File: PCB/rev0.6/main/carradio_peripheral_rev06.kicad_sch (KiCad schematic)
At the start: 205 parts, among them J1 ISO 10487 A (via pigtail), J10 K-line module socket, J12 Display buttons, J13 HDMI in (from VIM3), J14 Display FPC 40P 0.5mm, J18 VIM3 VIN (JST-XH 2P), J2 VIM3 40-pin via 2x20 IDC ribb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, J21 Expansion 2, J22 SWD, J23 Audio module socket, J25 USB module socket, J27 GNSS module socket, J5 VIM3 POWER key lead, J7 BH1750 light sensor, J8 ISO 10487 C1 (via pigtail), Q1 AO3400A, Q10 P-MOSFET -40V, Q11 CSD18543Q3A, Q12 CSD18543Q3A, Q2 P-MOSFET -60V, Q3 2N7002, SW1 BOOTSEL, SW2 RESET, U1 TPS560430XDBVR, U12 TPS55288RPMR, U13 CH334R, U19 AP2112K-3.3, U2 EL817S1(C), U20 RP2350B, U21 W25Q128JVS, U3 EL817S1(C), U4 EL817S1(C), U5 EL817S1(C), U6 LP5907MFX-3.3, Y1 12MHz, Y3 12MHz

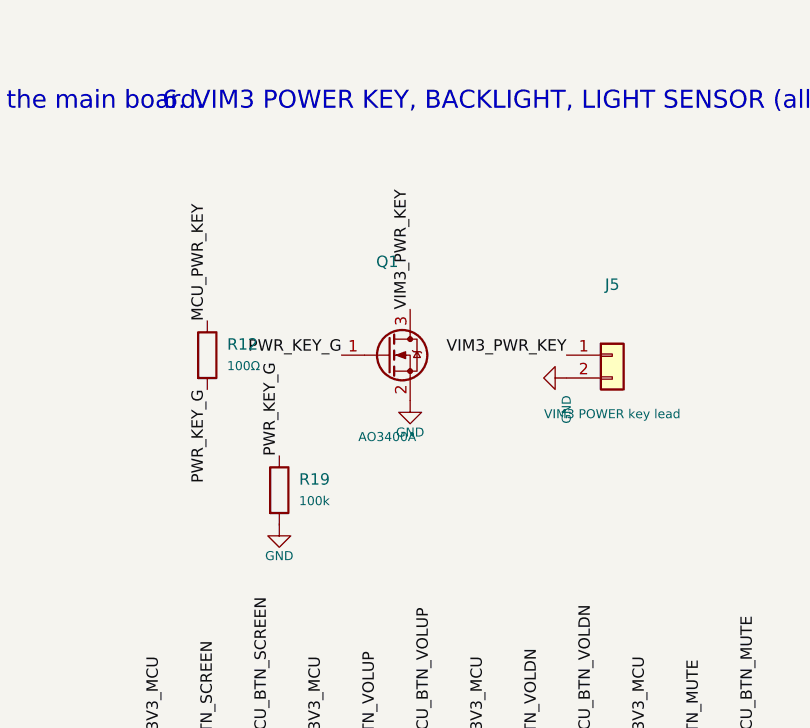
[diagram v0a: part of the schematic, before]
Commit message: PCB rev 0.6: VIM3 power key through a PhotoMOS (U22, AQY210S)
U22 shorts the two J5 pins (the VIM3 POWER key pads), isolated, instead of
Q1 pulling J5 pin 1 to GND. It sits on the bottom side next to J5; R12 is
now the 390 ohm LED resistor from GPIO15, R19 is gone. Schematic, board,
order files, LCSC list and docs updated. DRC: 0 unconnected, no errors.
bridge.py vias now use the board's 0.3 mm drill. A stale KiCad lock file is
untracked and *.lck ignored.

Co-Authored-By: Claude Opus 5.5 (1M context) <noreply@anthropic.com>
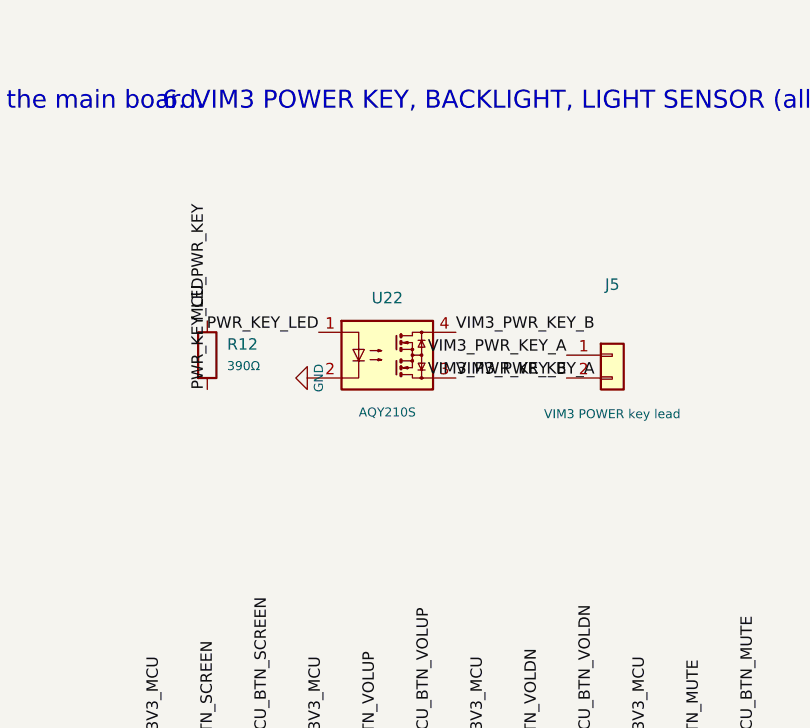
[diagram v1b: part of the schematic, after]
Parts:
- removed Q1: AO3400A, Package_TO_SOT_SMD:SOT-23, symbol Transistor_FET:AO3400A
- removed R19: 100k, Resistor_SMD:R_0603_1608Metric, symbol Device:R
- added U22: AQY210S, Package_SO:SO-4_4.4x4.3mm_P2.54mm, symbol Relay_SolidState:AQY210S
- R12: value 100Ω -> 390Ω; LCSC C22775 -> C23151; MPN 0603 100 1% -> UNI-ROYAL 0603WAF3900T5E 390 1%
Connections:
- net GND: now also U22.2; no longer J5.2 (Pin_2)
- net PWR_KEY_G renamed PWR_KEY_LED
- net PWR_KEY_LED: now also U22.1
- net VIM3_PWR_KEY renamed VIM3_PWR_KEY_A
- net VIM3_PWR_KEY_A: now also U22.3
- new net VIM3_PWR_KEY_B: J5.2 (Pin_2), U22.4
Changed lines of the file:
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@@
           (unit 1)))))
   (label
+    "PWR_KEY_LED"
+    (at 430 188.81 270)
+    (fields_autoplaced)
+    (effects
+      (font
+        (size 1.27 1.27))
+      (justify left bottom))
+)
+  (label
+    "PWR_KEY_LED"
+    (at 442.38 182.46 180)
+    (fields_autoplaced)
+    (effects
+      (font
+        (size 1.27 1.27))
+      (justify right bottom))
+)
+  (label
+    "VIM3_PWR_KEY_B"
+    (at 457.62 182.46 0)
+    (fields_autoplaced)
+    (effects
+      (font
+        (size 1.27 1.27))
+      (justify left bottom))
+)
+  (label
+    "VIM3_PWR_KEY_A"
+    (at 457.62 187.54 0)
+    (fields_autoplaced)
+    (effects
+      (font
+        (size 1.27 1.27))
+      (justify left bottom))
+)
+  (label
+    "VIM3_PWR_KEY_A"
+    (at 469.92 185 180)
+    (fields_autoplaced)
+    (effects
+      (font
+        (size 1.27 1.27))
+      (justify right bottom))
+)
+  (label
+    "VIM3_PWR_KEY_B"
+    (at 469.92 187.54 180)
+    (fields_autoplaced)
+    (effects
+      (font
+        (size 1.27 1.27))
+      (justify right bottom))
+)
+  (label
     "+3V3_MCU"
     (at 179.92 202.46 180)
@@
 )
   (symbol
-    (lib_id "Transistor_FET:AO3400A")
+    (lib_id "Relay_SolidState:AQY210S")
     (at 450 185 0)
     (unit 1)
@@
     (on_board yes)
     (dnp no)
-    (fields_autoplaced)
     (property
       "Reference"
-      "Q1"
-      (at 450 174.62 0)
+      "U22"
+      (at 450 178.65 0)
       (effects
         (font
@@
     (property
       "Value"
-      "AO3400A"
-      (at 450 194.08 0)
+      "AQY210S"
+      (at 450 191.35 0)
       (effects
         (font
@@
     (property
       "Footprint"
-      "Package_TO_SOT_SMD:SOT-23"
+      "Package_SO:SO-4_4.4x4.3mm_P2.54mm"
       (at 450 185 0)
       (effects
@@
     (property
       "LCSC"
-      "C20917"
+      ""
       (at 450 185 0)
       (effects
@@
     (property
       "MPN"
-      "AO3400A 30V 5.7A N-MOSFET"
+      "Panasonic AQY210S PhotoMOS 350V 120mA 1 Form A, SOP-4 (own stock)"
       (at 450 185 0)
       (effects
@@
       "3"
 )
+    (pin
+      "4"
+)
     (instances
       (project
@@
         (path
           "/3b49dff3-5af1-5299-8484-b6e3bf9b1595"
-          (reference "Q1")
+          (reference "U22")
           (unit 1)))))
-  (label
-    "PWR_KEY_G"
-    (at 444.92 185 180)
-    (fields_autoplaced)
-    (effects
-      (font
-        (size 1.27 1.27))
-      (justify right bottom))
-)
   (symbol
     (lib_id "power:GND")
-    (at 452.54 190.08 0)
+    (at 442.38 187.54 270)
     (unit 1)
     (in_bom no)
@@
       "Reference"
       "#PWR058"
-      (at 452.54 195.08 0)
+      (at 442.38 187.54 0)
       (effects
         (font
@@
       "Value"
       "GND"
-      (at 452.54 193.58 0)
+      (at 442.38 187.54 0)
       (effects
         (font
@@
       "Footprint"
       ""
-      (at 452.54 190.08 0)
+      (at 442.38 187.54 0)
       (effects
         (font
@@
       "Datasheet"
       ""
-      (at 452.54 190.08 0)
+      (at 442.38 187.54 0)
       (effects
         (font
@@
           (reference "#PWR058")
           (unit 1)))))
-  (label
-    "VIM3_PWR_KEY"
-    (at 452.54 179.92 90)
-    (fields_autoplaced)
-    (effects
-      (font
-        (size 1.27 1.27))
-      (justify left bottom))
-)
   (symbol
     (lib_id "Device:R")
@@
     (property
       "Value"
-      "100Ω"
+      "390Ω"
       (at 432.2 186.2 0)
       (effects
@@
     (property
       "LCSC"
-      "C22775"
+      "C23151"
       (at 430 185 0)
       (effects
@@
     (property
       "MPN"
-      "0603 100 1%"
+      "UNI-ROYAL 0603WAF3900T5E 390 1%"
       (at 430 185 0)
       (effects
@@
       (justify left bottom))
 )
-  (label
-    "PWR_KEY_G"
-    (at 430 188.81 270)
-    (fields_autoplaced)
-    (effects
-      (font
-        (size 1.27 1.27))
-      (justify right bottom))
-)
-  (symbol
-    (lib_id "Device:R")
-    (at 438 200 0)
-    (unit 1)
-    (in_bom yes)
-    (on_board yes)
-    (dnp no)
-    (fields_autoplaced)
-    (property
-      "Reference"
-      "R19"
-      (at 440.2 198.8 0)
-      (effects
-        (font
-          (size 1.27 1.27))
-        (justify left)))
-    (property
-      "Value"
-      "100k"
-      (at 440.2 201.2 0)
-      (effects
-        (font
-          (size 1 1))
-        (justify left)))
-    (property
-      "Footprint"
-      "Resistor_SMD:R_0603_1608Metric"
-      (at 438 200 0)
-      (effects
-        (font
-          (size 1.27 1.27))
-        hide))
-    (property
-      "Datasheet"
-      ""
-      (at 438 200 0)
-      (effects
-        (font
-          (size 1.27 1.27))
-        hide))
-    (property
-      "LCSC"
-      "C25803"
-      (at 438 200 0)
-      (effects
-        (font
-          (size 1.27 1.27))
-        hide))
-    (property
-      "MPN"
-      "0603 100k 1%"
-      (at 438 200 0)
-      (effects
-        (font
-          (size 1.27 1.27))
-        hide))
-    (pin
-      "1"
-)
-    (pin
-      "2"
-)
-    (instances
-      (project
-        "carradio_peripheral_rev06"
-        (path
-          "/3b49dff3-5af1-5299-8484-b6e3bf9b1595"
-          (reference "R19")
-          (unit 1)))))
-  (label
-    "PWR_KEY_G"
-    (at 438 196.19 90)
-    (fields_autoplaced)
-    (effects
-      (font
-        (size 1.27 1.27))
-      (justify left bottom))
-)
-  (symbol
-    (lib_id "power:GND")
-    (at 438 203.81 0)
-    (unit 1)
-    (in_bom no)
-    (on_board yes)
-    (dnp no)
-    (property
-      "Reference"
-      "#PWR059"
-      (at 438 208.81 0)
-      (effects
-        (font
-          (size 1.27 1.27))
-        hide))
-    (property
-      "Value"
-      "GND"
-      (at 438 207.31 0)
-      (effects
-        (font
-          (size 1 1))))
-    (property
-      "Footprint"
-      ""
-      (at 438 203.81 0)
-      (effects
-        (font
-          (size 1.27 1.27))
-        hide))
-    (property
-      "Datasheet"
-      ""
-      (at 438 203.81 0)
-      (effects
-        (font
-          (size 1.27 1.27))
-        hide))
-    (pin
-      "1"
-)
-    (instances
-      (project
-        "carradio_peripheral_rev06"
-        (path
-          "/3b49dff3-5af1-5299-8484-b6e3bf9b1595"
-          (reference "#PWR059")
-          (unit 1)))))
   (symbol
     (lib_id "Connector_Generic:Conn_01x02")
@@
           (reference "J5")
           (unit 1)))))
-  (label
-    "VIM3_PWR_KEY"
-    (at 469.92 185 180)
-    (fields_autoplaced)
-    (effects
-      (font
-        (size 1.27 1.27))
-      (justify right bottom))
-)
-  (symbol
-    (lib_id "power:GND")
-    (at 469.92 187.54 270)
-    (unit 1)
-    (in_bom no)
-    (on_board yes)
-    (dnp no)
-    (property
-      "Reference"
-      "#PWR060"
-      (at 469.92 192.54 0)
-      (effects
-        (font
-          (size 1.27 1.27))
-        hide))
-    (property
-      "Value"
-      "GND"
-      (at 469.92 191.04 0)
-      (effects
-        (font
-          (size 1 1))))
-    (property
-      "Footprint"
-      ""
-      (at 469.92 187.54 0)
-      (effects
-        (font
-          (size 1.27 1.27))
-        hide))
-    (property
-      "Datasheet"
-      ""
-      (at 469.92 187.54 0)
-      (effects
-        (font
-          (size 1.27 1.27))
-        hide))
-    (pin
-      "1"
-)
-    (instances
-      (project
-        "carradio_peripheral_rev06"
-        (path
-          "/3b49dff3-5af1-5299-8484-b6e3bf9b1595"
-          (reference "#PWR060")
-          (unit 1)))))
   (symbol

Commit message: PCB rev 0.6: 27 ohm resistors FOJAN FRC0603F27R0TS (C2907021)
UNI-ROYAL C25190 is backordered. Main board R83/R84 and GNSS R102/R103 use
the FOJAN 27 ohm 1% 0603 instead; BOMs, JLC BOMs and LCSC list updated.

Co-Authored-By: Claude Opus 5.5 (1M context) <noreply@anthropic.com>
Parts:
- R83, R84: LCSC C25190 -> C2907021; MPN UNI-ROYAL 0603WAF270JT5E 27R -> FOJAN FRC0603F27R0TS 27R 1%
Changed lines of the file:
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@@
     (property
       "LCSC"
-      "C25190"
+      "C2907021"
       (at 1060 230 0)
       (effects
@@
     (property
       "MPN"
-      "UNI-ROYAL 0603WAF270JT5E 27R"
+      "FOJAN FRC0603F27R0TS 27R 1%"
       (at 1060 230 0)
       (effects
@@
     (property
       "LCSC"
-      "C25190"
+      "C2907021"
       (at 1068 230 0)
       (effects
@@
     (property
       "MPN"
-      "UNI-ROYAL 0603WAF270JT5E 27R"
+      "FOJAN FRC0603F27R0TS 27R 1%"
       (at 1068 230 0)
       (effects
